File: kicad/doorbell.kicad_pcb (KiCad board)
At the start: 4 copper layers, 64 x 59 mm, 86 parts, among them J1 USB-C (USB4105), J2 WF26 bus, K1 GAQW212GS, K2 GAQY212GS, K3 GAQY412EH, K4 GAQY412EH, K5 G6K-2F-Y DC12, Q3 2N7002, Q4 2N7002, SW1 BOOT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

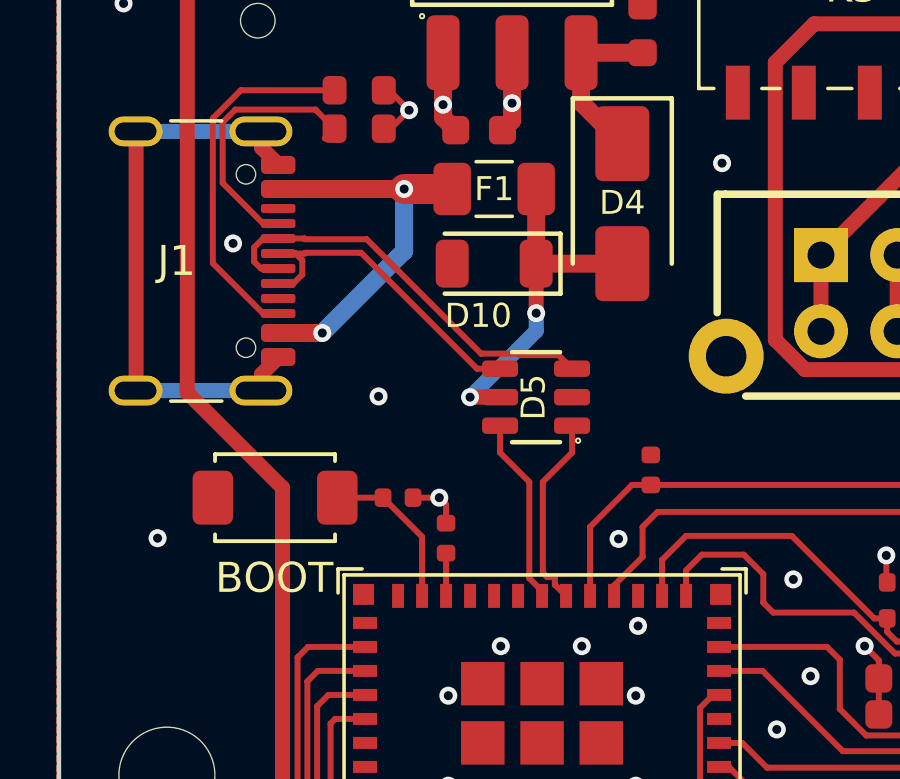
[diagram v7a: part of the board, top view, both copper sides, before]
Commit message: kicad: place USB ESD array (D5) at the connector + add C22 VCC bypass
Move D5 (TPD2S017) adjacent to J1 so the D+/D- ESD clamp sits right at
the USB-C port (routed D+/D- stub ~6-7 mm, single-layer F.Cu, no vias).
D5 VCC kept on VBUS_F (behind F1 + the D10 surge clamp); add C22
(0.1 uF 0603) as the local VCC bias bypass, VBUS_F -> GND at D5.
ERC clean (0 errors).

Claude-Session: https://claude.ai/code/session_01L7QeT64g2akf3TXKfsuiUZ
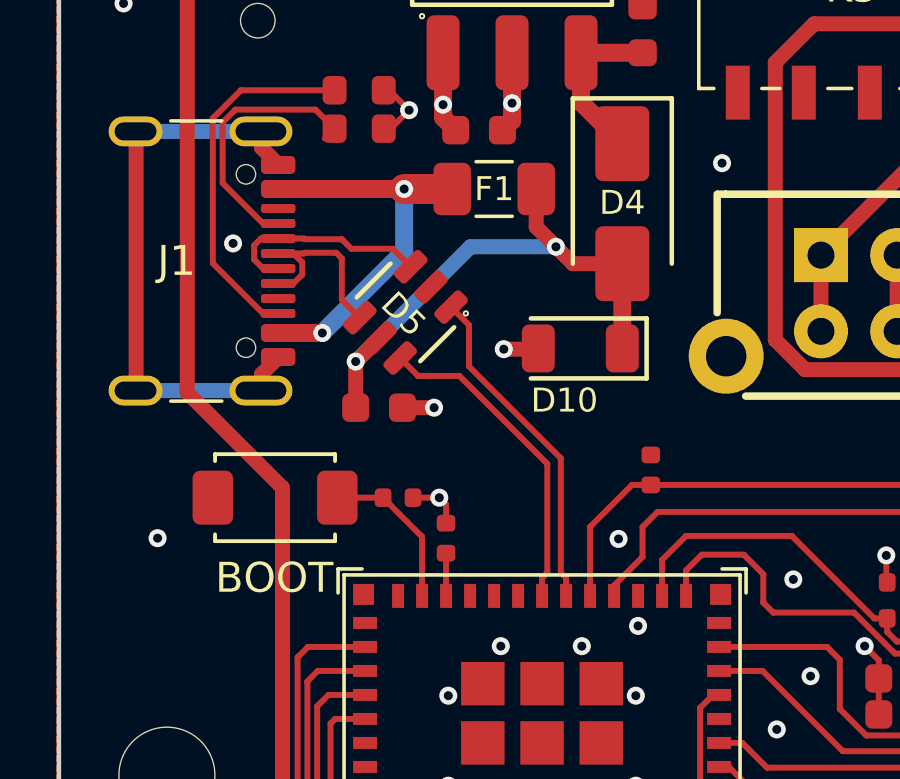
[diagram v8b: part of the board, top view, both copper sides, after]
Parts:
- added C22: 100nF, PCM_JLCPCB:C_0603, F.Cu at (27.1, 37.0)
- moved D5 5.19 mm to (28.0, 33.8), turned to 135 degrees
- moved D10 4.03 mm to (33.9, 35.0)
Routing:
- net /USB_DN: track 13.9 -> 7.10 mm
- net /VBUS_F: track 11.8 -> 18.4 mm
- net /USB_ESP_DN: track 6.55 -> 11.2 mm
- net /USB_DP: track 11.3 -> 6.69 mm
- net /USB_ESP_DP: track 6.25 -> 10.8 mm
- net GND: track 52.8 -> 55.0 mm, vias 59 -> 60
